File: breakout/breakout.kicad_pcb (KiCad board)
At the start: 2 copper layers, 75 x 48 mm, 10 parts, among them J1 Glasgow, J2 ScrewTerminals, J3 SignalsMale, J4 SignalsFemale, J5 SignalsMale, J6 SignalsFemale, J7 TestPoints, J9 FX2LA

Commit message: finished
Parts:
- J2: footprint TerminalBlock_Phoenix:TerminalBlock_Phoenix_MPT-0,5-12-2.54_1x12_P2.54mm_Horizontal -> Glasgow:TerminalBlock_not_WAGO_233-512_2x12_P2.54mm
- moved J2 4.20 mm to (185.2, 72.4)
- moved H1 2.50 mm to (191.5, 66.0)
- moved H2 2.50 mm to (191.5, 106.0)
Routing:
- net VBUS: track 45.2 -> 49.4 mm
- net /D1: track 57.4 -> 61.6 mm
- net /D5: track 57.1 -> 61.3 mm
- net /D7: track 59.2 -> 63.4 mm
- net /D3: track 55.7 -> 59.9 mm
- net /D4: track 53.0 -> 57.2 mm
- net /D2: track 53.2 -> 57.4 mm
- net /D6: track 54.1 -> 58.3 mm
- net /D0: track 54.9 -> 59.1 mm
- net /VSENSE: track 48.6 -> 52.8 mm
- net GND: vias 155 -> 165
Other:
- board size 75 x 48 mm -> 80 x 48 mm

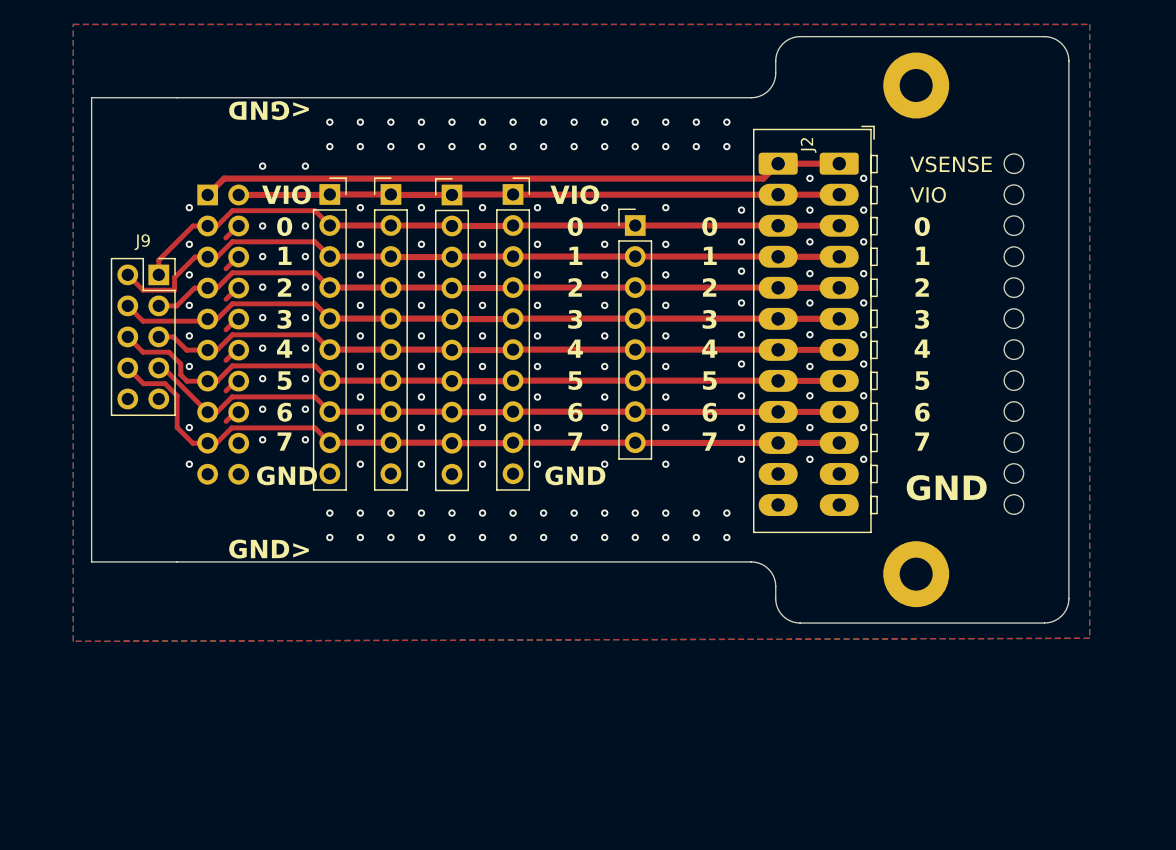
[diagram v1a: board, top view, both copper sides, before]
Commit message: wip? rev2
- rounded corners
- more LA space (todo confirm spacing re: glasgow center)
- vio/vsense connection switch
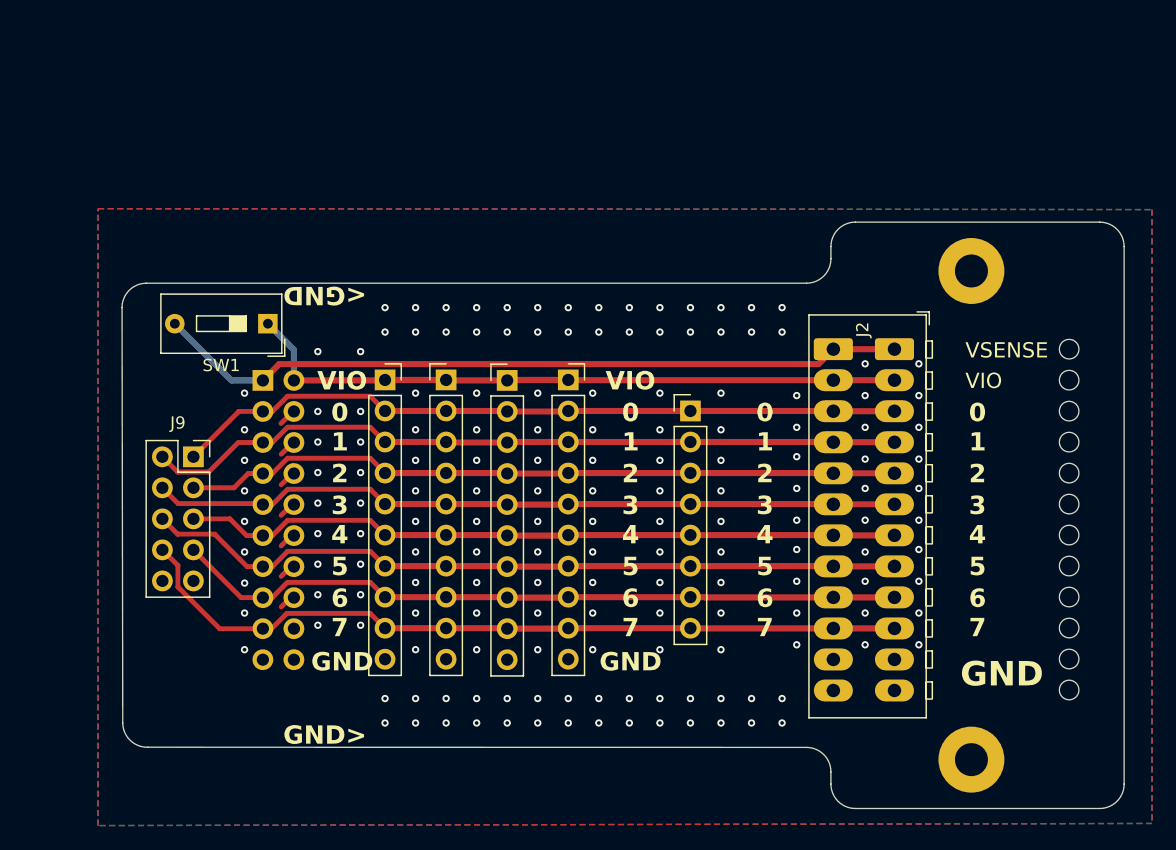
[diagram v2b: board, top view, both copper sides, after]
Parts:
- added SW1: SW_SPST, Button_Switch_THT:SW_DIP_SPSTx01_Slide_9.78x4.72mm_W7.62mm_P2.54mm, F.Cu at (138.4, 85.5)
- moved J2 15.8 mm to (189.7, 87.6)
- moved H1 15.8 mm to (196.0, 81.2)
- moved H2 15.8 mm to (196.0, 121.2)
- moved J1 15.8 mm to (138.0, 90.1)
- moved J3 15.8 mm to (153.0, 90.1)
- moved J4 15.8 mm to (148.0, 90.1)
- moved J5 15.8 mm to (158.0, 90.1)
- moved J6 15.8 mm to (163.0, 90.1)
- moved J7 15.8 mm to (173.0, 92.6)
- moved J9 15.2 mm to (132.3, 96.4)
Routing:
- net /VSENSE: track 52.8 -> 61.9 mm
- net VBUS: track 49.4 -> 54.9 mm
- net /D3: track 59.9 -> 61.8 mm
- net /D6: track 58.3 -> 60.1 mm
- net /D4: track 57.2 -> 59.0 mm
- net /D2: track 57.4 -> 58.9 mm
- net /D7: track 63.4 -> 64.7 mm
- net /D5: track 61.3 -> 62.6 mm
- net /D1: track 61.6 -> 62.6 mm
- net /D0: track 59.1 -> 60.0 mm
- net GND: vias 165 -> 166
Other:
- board size 80 x 48 mm -> 82 x 48 mm
